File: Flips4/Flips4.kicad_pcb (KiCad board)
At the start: 2 copper layers, 21 x 61.6 mm, 4 parts, among them CN1 Conn_02x05_Odd_Even, CN2 Conn_02x16_Counter_Clockwise, U1 FP2800A

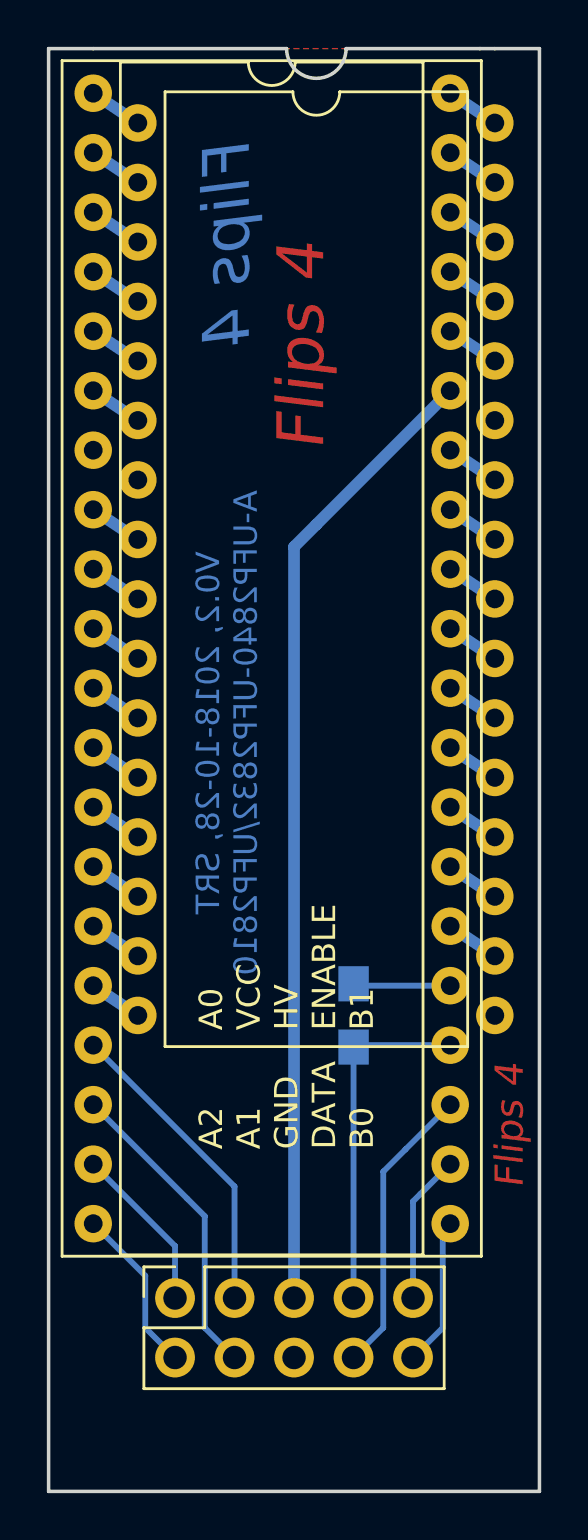
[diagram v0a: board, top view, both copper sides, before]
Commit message: using own UFP2810 connector
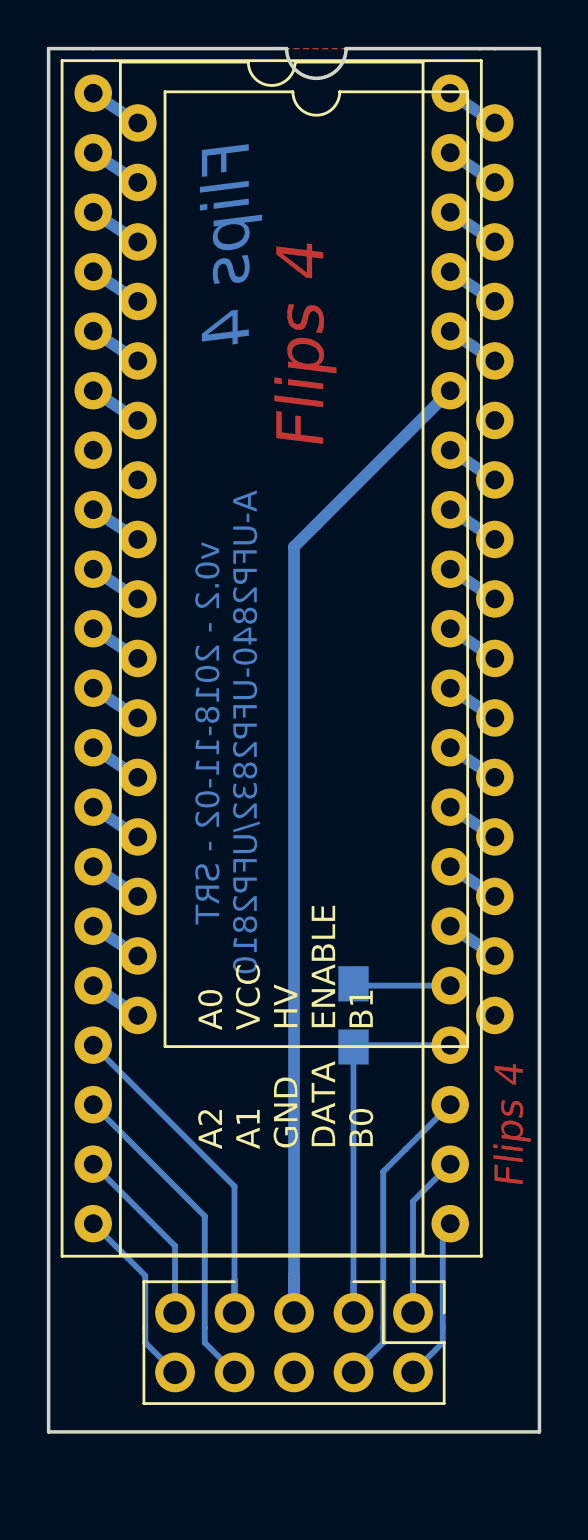
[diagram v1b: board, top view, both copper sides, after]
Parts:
- CN1: value Conn_02x05_Odd_Even -> UFP2810; footprint Socket_Strips:Socket_Strip_Straight_2x05_Pitch2.54mm -> Own:Pin_Header_Angle_Shrouded_2x05_Pitch2.54mm
- moved CN1 10.2 mm to (234.0, 118.7), turned to 270 degrees
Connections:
- CN1 pad 1: /A0 -> /B1
- CN1 pad 10: /B0 -> /A2
- CN1 pad 2: /A2 -> /B0
- CN1 pad 3: VCC -> /Enable
- CN1 pad 4: /A1 -> /Data
- CN1 pad 7: /Enable -> VCC
- CN1 pad 8: /Data -> /A1
- CN1 pad 9: /B1 -> /A0
- CN2 pad 17: Net-(CN2-Pad17) -> (no net)
- CN2 pad 27: Net-(CN2-Pad27) -> (no net)
- CN2 pad 7: Net-(CN2-Pad7) -> (no net)
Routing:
- net +12V: track 41.5 -> 43.1 mm
- net VCC: track 13.3 -> 14.7 mm
- net /Enable: track 14.9 -> 16.3 mm
- net /A0: track 7.16 -> 8.37 mm
- net /B1: track 6.37 -> 7.52 mm
- net /Data: track 12.5 -> 13.1 mm
- net /B0: track 6.82 -> 7.46 mm
- net /A2: track 7.16 -> 7.80 mm
- net /A1: track 13.3 -> 13.9 mm
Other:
- board size 21 x 61.6 mm -> 21 x 59.1 mm
- board text added: "v0.2 - 2018-11-02 - SRT A-UFP2840-UFP2832/UFP2810"
- board text removed: "V0.2, 2018-10-28, SRT A-UFP2840-UFP2832/UFP2810"

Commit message: rework inscriptions
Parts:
- added REF**: KiCAD Logo, Symbols:Symbol_KiCAD-Logo_CopperAndSilkScreenTop, B.Cu at (231.6, 91.9)
- added REF***: WEEE-Logo_4.2x6mm_SilkScreen, Symbols:WEEE-Logo_4.2x6mm_SilkScreen, B.Cu at (231.1, 113.8)
- added REF***: OSHW-Logo2_7.3x6mm_SilkScreen, Symbols:OSHW-Logo2_7.3x6mm_SilkScreen, B.Cu at (231.6, 80.8)
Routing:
- added copper zone on B.Cu, net (none)
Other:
- outline, holes or cut-outs redrawn
- board text added: "FLIPS"
- board text added: "SRT Flips 4 V1.0"
- board text added: "SRT Flips 4 V1.0 2018-11-03 github.com/cawapy/FlipSuite"
- board text removed: "A0 VCC HV ENABLE B1"
- board text removed: "A2 A1 GND DATA B0"
- board text removed: "Flips 4"
- board text removed: "v0.2 - 2018-11-02 - SRT A-UFP2840-UFP2832/UFP2810"
